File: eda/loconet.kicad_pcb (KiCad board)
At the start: 2 copper layers, 105.7 x 60.2 mm, 73 parts, among them J1 RJ12, J10 FROG4, J11 LN Debug, J12 LN Raw, J13 Input voltage, J14 IO, J15 Power, J2 DCC IN, J3 FROG1, J4 DCC1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

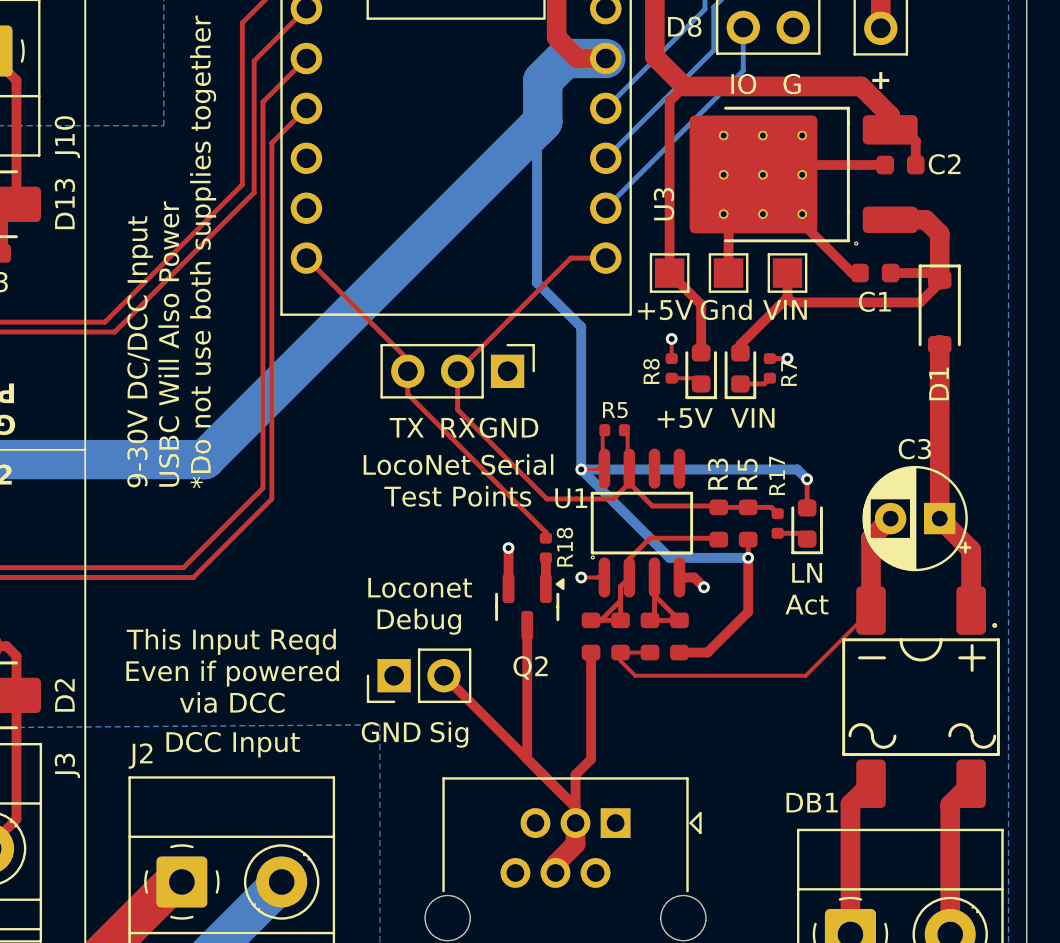
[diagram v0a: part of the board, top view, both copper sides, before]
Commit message: Mostly works now, but there is still at least one issue.
* PCB seems to work just fine for reading inputs, and can communicate with a DCS52
* Code has been tweaked a bit, and the inverted parameters are weird, but opposites work
* For whatever reason, when I plug in the USB to DCS52 and connect JMRI, this all goes to hell
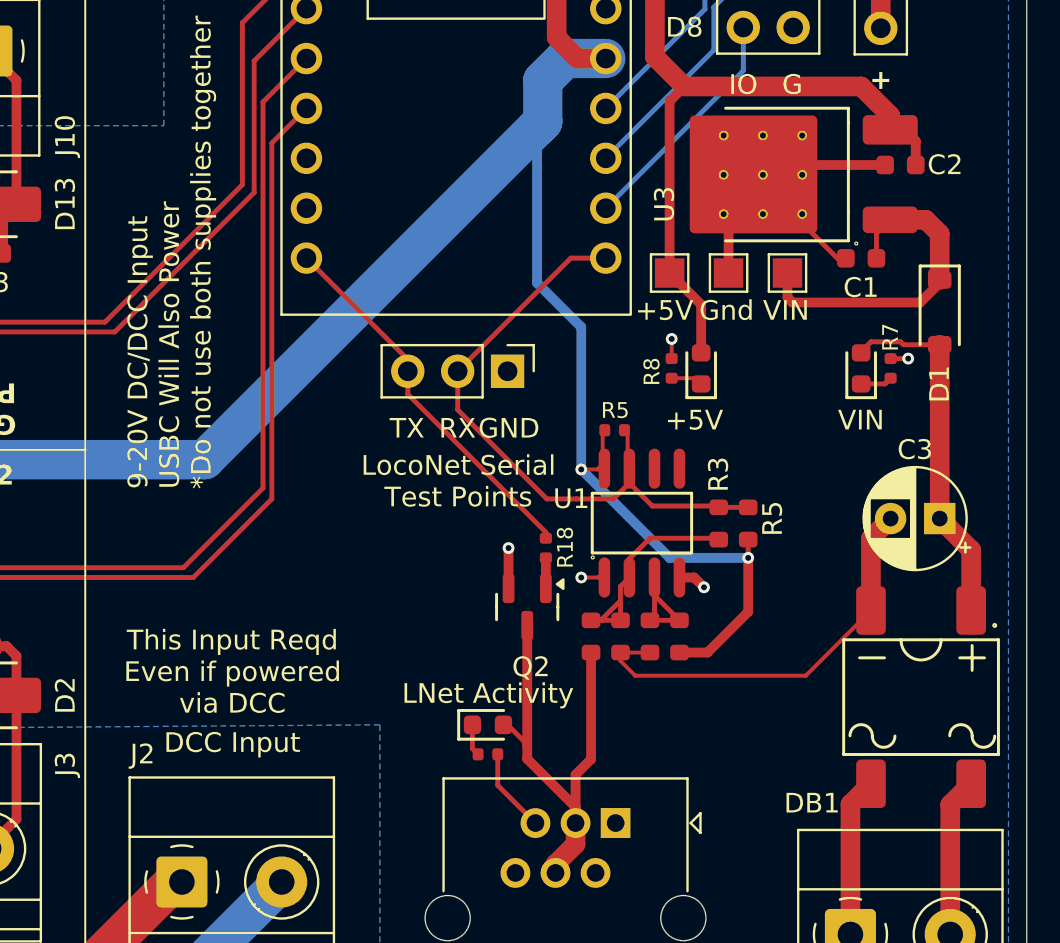
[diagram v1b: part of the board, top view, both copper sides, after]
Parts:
- removed J12: LN Raw, Connector_PinHeader_2.54mm:PinHeader_1x02_P2.54mm_Vertical
- removed R17: 1kΩ, PCM_JLCPCB:R_0402
- added R25: 2kΩ, PCM_JLCPCB:R_0402, F.Cu at (171.0, 117.0)
- moved D16 19.2 mm to (171.0, 115.5), turned to 0 degrees
- moved D6 6.15 mm to (190.0, 97.4)
- moved R7 6.15 mm to (191.5, 97.4)
- moved C1 1.04 mm to (190.0, 91.8)
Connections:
- D16 pad 2: +3V3 -> /LNET
- D6 pad 2: Net-(U3-VIN) -> Net-(DB1-+)
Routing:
- net +3V3: track 187.5 -> 174.3 mm, vias 7 -> 6
- net /LNET: track 35.4 -> 24.7 mm
- net Net-(DB1-+): track 14.2 -> 18.5 mm
- net Net-(U3-VIN): track 21.3 -> 17.6 mm
- net GND: track 57.2 -> 60.5 mm
- net RX: track 35.3 -> 33.7 mm
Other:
- board text added: "9-20V DC/DCC Input USBC Will Also Power *Do not use both supplies together"
- board text added: "LNet Activity"
- board text removed: "9-30V DC/DCC Input USBC Will Also Power *Do not use both supplies together"
- board text removed: "LN Act"
- board text removed: "Loconet Debug"
- board text removed: "Sig"
